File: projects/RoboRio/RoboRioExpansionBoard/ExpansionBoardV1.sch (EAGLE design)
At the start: 115 parts, among them IC1 MC1525TO, IC2 74HCT125N, Q1 5MHz

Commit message: Brokout 12 IO pins.
Was fun
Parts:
- removed IO0-SPI-CS, IO1-SPI-CLK, IO12, IO13, IO14, IO15, IO16, IO17, IO18, IO19, IO2-SPI-MOSI, IO20, IO21, IO22, IO23, IO24, IO25, IO26, IO27, IO3-SPI-MISO: (no value), con-lstb-modified:MA03-1
- added IO0, IO1, IO2, IO3: (no value), con-lstb-modified:MA03-1
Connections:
- new net IO28: IO5.3
- new net IO29: IO6.3
- new net IO30: IO7.3
- new net IO31: IO8.3
- new net IO32: IO9.3
- new net IO33: IO10.3
- new net IO34: IO11.3
- new net IO4: IO4.3
- net +3V3: now also IO0.2, IO1.2, IO2.2, IO3.2; no longer IO0-SPI-CS.2, IO1-SPI-CLK.2, IO12.2, IO13.2, IO14.2, IO15.2, IO16.2, IO17.2, IO18.2, IO19.2, IO2-SPI-MOSI.2, IO20.2, IO21.2, IO22.2, IO23.2, IO24.2, IO25.2, IO26.2, IO27.2, IO3-SPI-MISO.2
- net DGND: now also IO0.1, IO1.1, IO2.1, IO3.1; no longer IO0-SPI-CS.1, IO1-SPI-CLK.1, IO12.1, IO13.1, IO14.1, IO15.1, IO16.1, IO17.1, IO18.1, IO19.1, IO2-SPI-MOSI.1, IO20.1, IO21.1, IO22.1, IO23.1, IO24.1, IO25.1, IO26.1, IO27.1, IO3-SPI-MISO.1
- net IO0: now also IO0.3
- net IO1: now also IO1.3
- net IO10: no longer IO10.3
- net IO11: no longer IO11.3
- net IO12: no longer IO12.3
- net IO13: no longer IO13.3
- net IO14: no longer IO14.3
- net IO15: no longer IO15.3
- net IO16: no longer IO16.3
- net IO17: no longer IO17.3
- net IO18: no longer IO18.3
- net IO19: no longer IO19.3
- net IO2: now also IO2.3
- net IO20: no longer IO20.3
- net IO21: no longer IO21.3
- net IO22: no longer IO22.3
- net IO23: no longer IO23.3
- net IO24: no longer IO24.3
- net IO25: no longer IO25.3
- net IO26: no longer IO26.3
- net IO27: no longer IO27.3
- net IO3: now also IO3.3
- net IO4RRW: no longer IO4.3
- net IO5: no longer IO5.3
- net IO6: no longer IO6.3
- net IO7: no longer IO7.3
- net IO8: no longer IO8.3
- net IO9: no longer IO9.3
- net SPI_CLK: no longer IO1-SPI-CLK.3
- net SPI_CS: no longer IO0-SPI-CS.3
- net SPI_MISO: no longer IO3-SPI-MISO.3
- net SPI_MOSI: no longer IO2-SPI-MOSI.3
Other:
- moved on the sheet: IO10, IO11, IO4, IO5, IO6, IO7, IO8, IO9

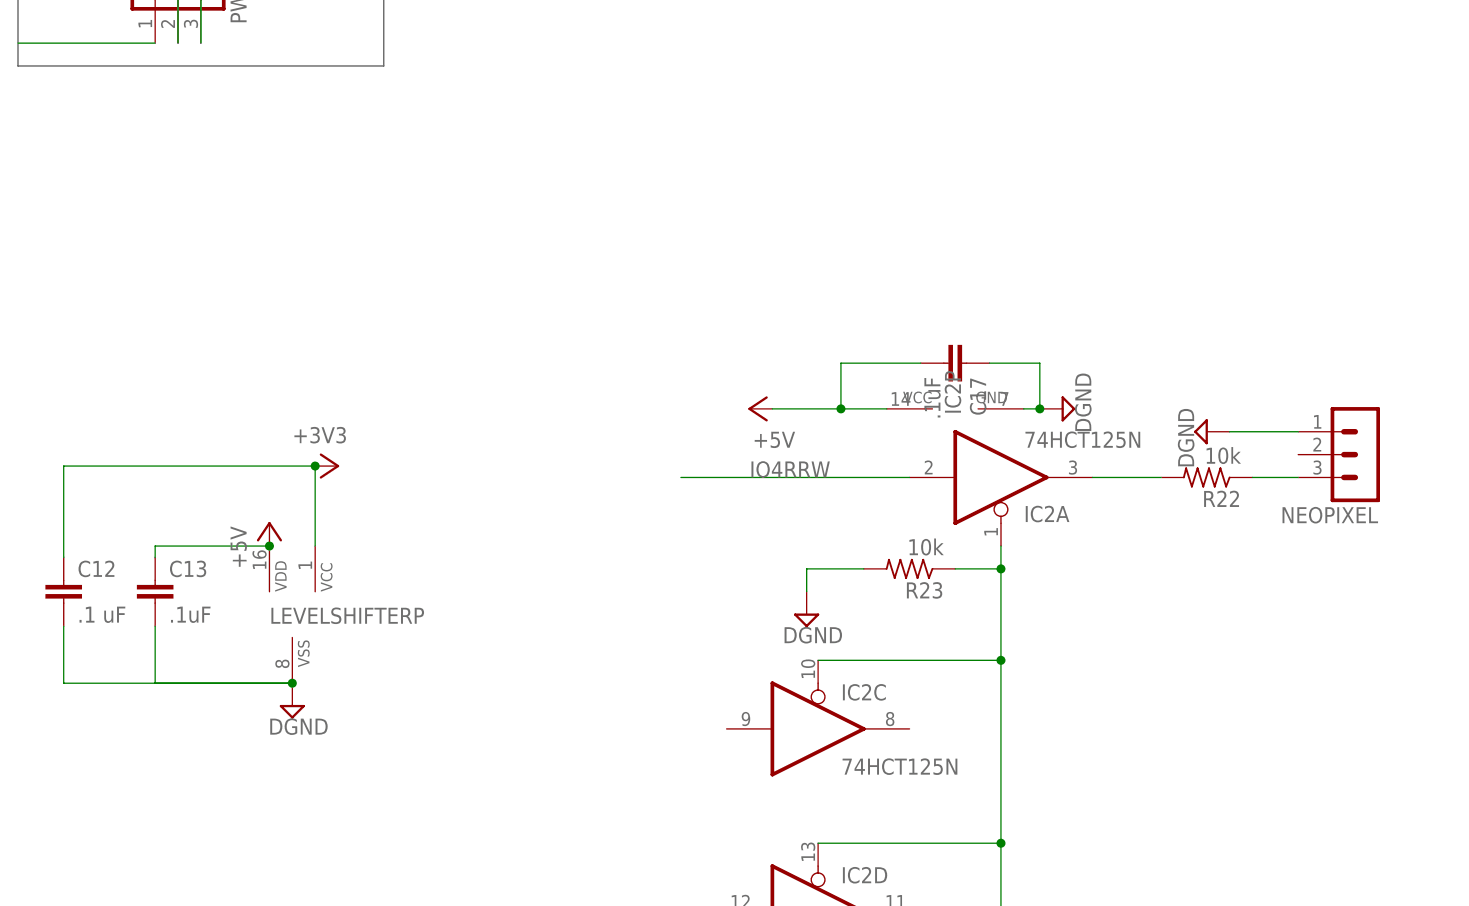
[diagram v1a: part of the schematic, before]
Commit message: Updated neopixel stuff
Not yet finished.
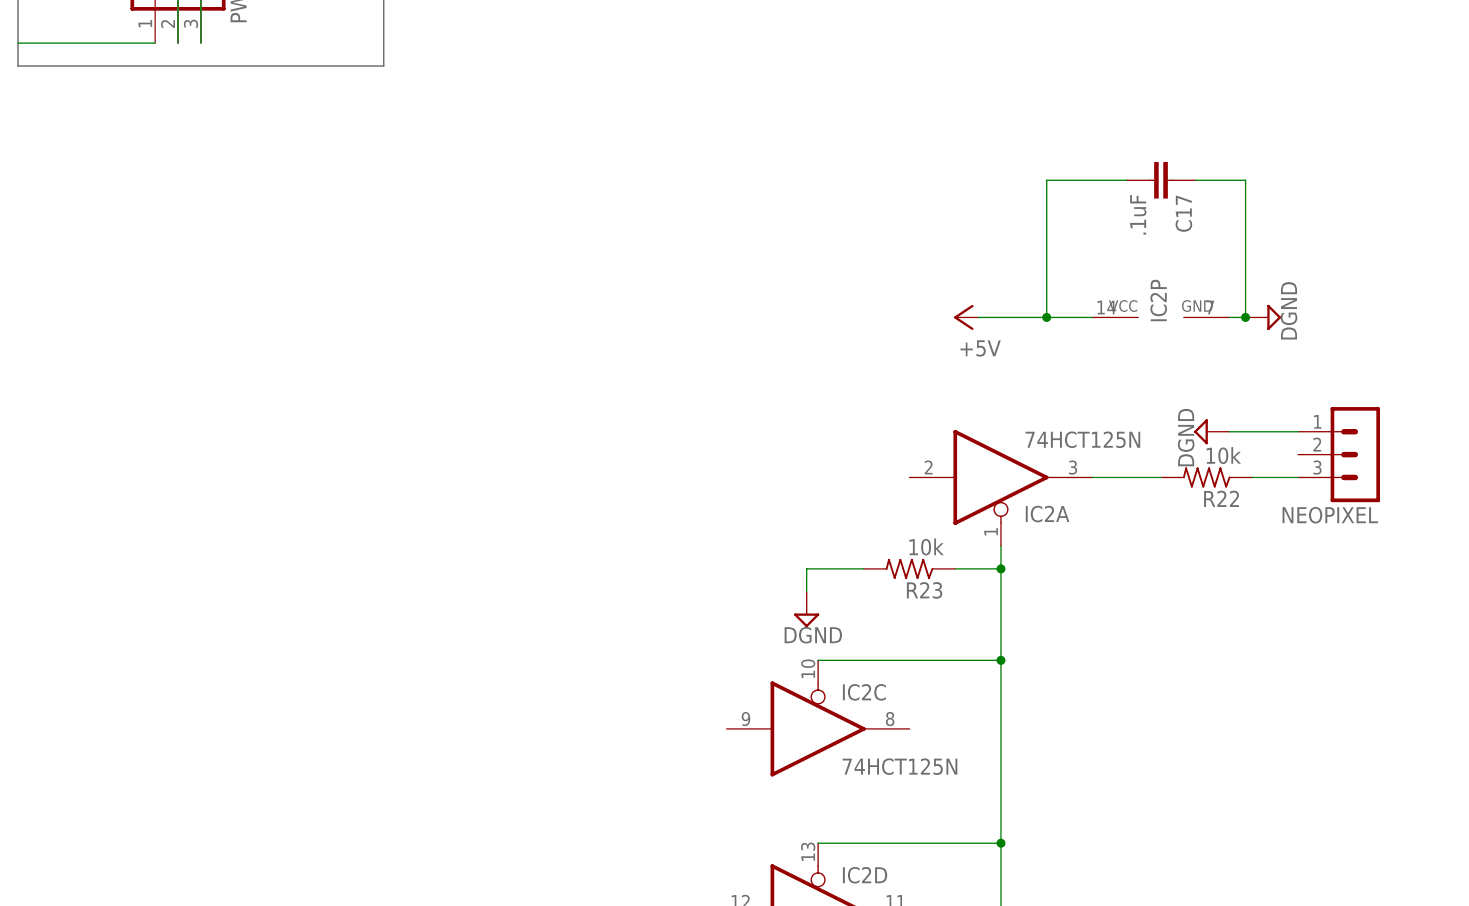
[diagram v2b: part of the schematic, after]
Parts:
- removed C12: .1 uF, capacitor-wima:C7.5/6
- removed C13: .1uF, capacitor-wima:C7.5/6
- removed LEVELSHIFTER: 40109, 40xx-2:40109
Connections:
- net +3V3: no longer C12.1, LEVELSHIFTERP.VCC
- net +5V: no longer C13.1, LEVELSHIFTERP.VDD
- net DGND: no longer C12.2, C13.2, LEVELSHIFTERP.VSS
- net IO4RRW: no longer IC2A.I
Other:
- moved on the sheet: C17, IC2P
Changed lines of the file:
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@@
 <part name="PWM9" library="con-lstb-modified" deviceset="MA03-1" device=""/>
 <part name="ADC" library="adafruit" deviceset="MCP3008" device=""/>
-<part name="LEVELSHIFTER" library="40xx-2" deviceset="40109" device=""/>
 <part name="NEOPIXEL" library="con-lstb-modified" deviceset="MA03-1" device=""/>
-<part name="P+12" library="supply1" deviceset="+5V" device=""/>
-<part name="+3V6" library="supply1" deviceset="+3V3" device=""/>
 <part name="R2" library="resistor" deviceset="R-US_" device="0309/V" value="150"/>
 <part name="R3" library="resistor" deviceset="R-US_" device="0309/V" value="150"/>
@@
 <part name="U$4" library="RESETBUTTON3000" deviceset="BUTTON" device=""/>
 <part name="C2" library="capacitor-wima" deviceset="C" device="7.5/6" value=".1uF"/>
-<part name="C12" library="capacitor-wima" deviceset="C" device="7.5/6" value=".1 uF"/>
-<part name="C13" library="capacitor-wima" deviceset="C" device="7.5/6" value=".1uF"/>
 <part name="AI2" library="con-lstb-modified" deviceset="MA03-1" device=""/>
 <part name="AI3" library="con-lstb-modified" deviceset="MA03-1" device=""/>
@@
 <part name="SUPPLY13" library="supply2" deviceset="DGND" device=""/>
 <part name="SUPPLY14" library="supply2" deviceset="DGND" device=""/>
-<part name="SUPPLY15" library="supply2" deviceset="DGND" device=""/>
 <part name="SUPPLY18" library="supply2" deviceset="DGND" device=""/>
 <part name="ADC0" library="con-lstb-modified" deviceset="MA03-1" device=""/>
@@
 <instance part="PWM9" gate="G$1" x="-355.6" y="0" rot="R270"/>
 <instance part="ADC" gate="G$1" x="-7.62" y="-83.82" rot="R180"/>
-<instance part="LEVELSHIFTER" gate="P" x="-342.9" y="-71.12"/>
 <instance part="NEOPIXEL" gate="G$1" x="-223.52" y="-53.34" rot="R180"/>
-<instance part="P+12" gate="1" x="-345.44" y="-60.96"/>
-<instance part="+3V6" gate="G$1" x="-337.82" y="-54.61" rot="R270"/>
 <instance part="R2" gate="G$1" x="-71.12" y="149.86" rot="R180"/>
 <instance part="R3" gate="G$1" x="-71.12" y="160.02" rot="R180"/>
@@
 <instance part="U$4" gate="G$1" x="27.94" y="101.6"/>
 <instance part="C2" gate="G$1" x="-55.88" y="68.58" rot="R90"/>
-<instance part="C12" gate="G$1" x="-368.3" y="-67.31"/>
-<instance part="C13" gate="G$1" x="-358.14" y="-67.31"/>
 <instance part="AI2" gate="G$1" x="-189.23" y="45.72" rot="R180"/>
 <instance part="AI3" gate="G$1" x="-189.23" y="31.75" rot="R180"/>
@@
 <instance part="SUPPLY13" gate="G$1" x="36.83" y="-27.94"/>
 <instance part="SUPPLY14" gate="G$1" x="-241.3" y="-50.8" rot="R270"/>
-<instance part="SUPPLY15" gate="G$1" x="-342.9" y="-81.28"/>
 <instance part="SUPPLY18" gate="G$1" x="-259.08" y="27.94"/>
 <instance part="ADC0" gate="G$1" x="71.12" y="-266.7" rot="R180"/>
@@
 <instance part="IC2" gate="C" x="-284.48" y="-83.82"/>
 <instance part="IC2" gate="D" x="-284.48" y="-104.14"/>
-<instance part="IC2" gate="P" x="-269.24" y="-48.26" rot="R90"/>
+<instance part="IC2" gate="P" x="-246.38" y="-38.1" rot="R90"/>
 <instance part="SUPPLY37" gate="G$1" x="-285.75" y="-71.12"/>
-<instance part="P+4" gate="1" x="-292.1" y="-48.26" rot="R90"/>
-<instance part="C17" gate="G$1" x="-267.97" y="-43.18" rot="R270"/>
-<instance part="SUPPLY38" gate="G$1" x="-257.302" y="-48.26" rot="R90"/>
+<instance part="P+4" gate="1" x="-269.24" y="-38.1" rot="R90"/>
+<instance part="C17" gate="G$1" x="-245.11" y="-22.86" rot="R270"/>
+<instance part="SUPPLY38" gate="G$1" x="-234.442" y="-38.1" rot="R90"/>
 <instance part="ADC1" gate="G$1" x="71.12" y="-236.22" rot="R180"/>
 <instance part="R6" gate="G$1" x="55.88" y="-238.76" rot="MR180"/>
@@
 </segment>
 <segment>
-<pinref part="LEVELSHIFTER" gate="P" pin="VCC"/>
-<pinref part="+3V6" gate="G$1" pin="+3V3"/>
-<pinref part="C12" gate="G$1" pin="1"/>
-<wire x1="-340.36" y1="-54.61" x2="-340.36" y2="-63.5" width="0.1524" layer="91"/>
-<junction x="-340.36" y="-54.61"/>
-<wire x1="-340.36" y1="-54.61" x2="-368.3" y2="-54.61" width="0.1524" layer="91"/>
-<wire x1="-368.3" y1="-54.61" x2="-368.3" y2="-64.77" width="0.1524" layer="91"/>
-</segment>
-<segment>
 <pinref part="U$6" gate="G$1" pin="VDD"/>
 <pinref part="+3V5" gate="G$1" pin="+3V3"/>
@@
 <wire x1="-83.82" y1="40.64" x2="-63.5" y2="40.64" width="0.1524" layer="91"/>
 <label x="-81.28" y="40.64" size="1.778" layer="95"/>
-</segment>
-<segment>
-<wire x1="-299.72" y1="-55.88" x2="-274.32" y2="-55.88" width="0.1524" layer="91"/>
-<label x="-292.1" y="-55.88" size="1.778" layer="95"/>
-<pinref part="IC2" gate="A" pin="I"/>
 </segment>
 </net>
@@
 </segment>
 <segment>
-<pinref part="LEVELSHIFTER" gate="P" pin="VDD"/>
-<pinref part="P+12" gate="1" pin="+5V"/>
-<wire x1="-345.44" y1="-63.5" x2="-358.14" y2="-63.5" width="0.1524" layer="91"/>
-<wire x1="-358.14" y1="-63.5" x2="-358.14" y2="-64.77" width="0.1524" layer="91"/>
-<pinref part="C13" gate="G$1" pin="1"/>
-<junction x="-345.44" y="-63.5"/>
-</segment>
-<segment>
 <pinref part="5V_LCD" gate="G$1" pin="2"/>
 <wire x1="33.02" y1="-34.29" x2="36.83" y2="-38.1" width="0.1524" layer="91"/>
@@
 <segment>
 <pinref part="P+4" gate="1" pin="+5V"/>
-<wire x1="-289.56" y1="-48.26" x2="-281.94" y2="-48.26" width="0.1524" layer="91"/>
-<wire x1="-281.94" y1="-48.26" x2="-281.94" y2="-43.18" width="0.1524" layer="91"/>
+<wire x1="-266.7" y1="-38.1" x2="-259.08" y2="-38.1" width="0.1524" layer="91"/>
+<wire x1="-259.08" y1="-38.1" x2="-259.08" y2="-22.86" width="0.1524" layer="91"/>
 <pinref part="C17" gate="G$1" pin="2"/>
-<wire x1="-273.05" y1="-43.18" x2="-281.94" y2="-43.18" width="0.1524" layer="91"/>
+<wire x1="-250.19" y1="-22.86" x2="-259.08" y2="-22.86" width="0.1524" layer="91"/>
 <pinref part="IC2" gate="P" pin="VCC"/>
-<wire x1="-281.94" y1="-48.26" x2="-276.86" y2="-48.26" width="0.1524" layer="91"/>
-<junction x="-281.94" y="-48.26"/>
+<wire x1="-259.08" y1="-38.1" x2="-254" y2="-38.1" width="0.1524" layer="91"/>
+<junction x="-259.08" y="-38.1"/>
 </segment>
 <segment>
@@
 </segment>
 <segment>
-<pinref part="LEVELSHIFTER" gate="P" pin="VSS"/>
-<pinref part="C12" gate="G$1" pin="2"/>
-<junction x="-342.9" y="-78.74"/>
-<wire x1="-342.9" y1="-78.74" x2="-368.3" y2="-78.74" width="0.1524" layer="91"/>
-<wire x1="-368.3" y1="-78.74" x2="-368.3" y2="-72.39" width="0.1524" layer="91"/>
-<pinref part="C13" gate="G$1" pin="2"/>
-<wire x1="-342.9" y1="-78.74" x2="-358.14" y2="-78.74" width="0.1524" layer="91"/>
-<wire x1="-358.14" y1="-78.74" x2="-358.14" y2="-72.39" width="0.1524" layer="91"/>
-<pinref part="SUPPLY15" gate="G$1" pin="DGND"/>
-</segment>
-<segment>
 <pinref part="U$1" gate="G$1" pin="8-DGND"/>
 <pinref part="U$1" gate="G$1" pin="16-DGND"/>
@@
 <segment>
 <pinref part="C17" gate="G$1" pin="1"/>
-<wire x1="-265.43" y1="-43.18" x2="-259.842" y2="-43.18" width="0.1524" layer="91"/>
+<wire x1="-242.57" y1="-22.86" x2="-236.982" y2="-22.86" width="0.1524" layer="91"/>
 <pinref part="IC2" gate="P" pin="GND"/>
-<wire x1="-259.842" y1="-43.18" x2="-259.842" y2="-48.26" width="0.1524" layer="91"/>
-<wire x1="-259.842" y1="-48.26" x2="-261.62" y2="-48.26" width="0.1524" layer="91"/>
+<wire x1="-236.982" y1="-22.86" x2="-236.982" y2="-38.1" width="0.1524" layer="91"/>
+<wire x1="-236.982" y1="-38.1" x2="-238.76" y2="-38.1" width="0.1524" layer="91"/>
 <pinref part="SUPPLY38" gate="G$1" pin="DGND"/>
-<junction x="-259.842" y="-48.26"/>
-</segment>
-<segment>
+<junction x="-236.982" y="-38.1"/>
+</segment>
+<segment>

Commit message: Were almost there......
"if your going through boring schematic checking, keep going"-Winston
Churchill
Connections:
- removed net IO28: IO5.3
- removed net IO29: IO6.3
- removed net IO30: IO7.3
- removed net IO31: IO8.3
- removed net IO32: IO9.3
- removed net IO33: IO10.3
- removed net IO34: IO11.3
- removed net IO4RRW: PROPELLERP8X32A-D40.P4
- removed net N$18: ADC.CH2
- removed net N$19: ADC.CH3
- removed net N$21: RN1.2, U$6.DAT2
- removed net N$23: C7.1, R11.1, R12.2
- removed net N$28: C8.1, R13.1, R14.2
- removed net N$32: C11.1, R20.1, R21.2
- removed net N$43: ADC.CH4
- removed net N$6: C4.1, R6.1, R8.2
- removed net SPI_CLK: U$1.21-IO5-SPI_CLK
- removed net SPI_CS: U$1.19-IO4-SPI_CS
- removed net SPI_MISO: U$1.23-IO4-SPI_MISO
- removed net SPI_MOSI: U$1.25-IO7-SPI_MOSI
- new net N$17: ADC.CH4, C8.1, R13.1, R14.2
- net IO0: now also U$1.19-IO4-SPI_CS
- net IO1: now also U$1.21-IO5-SPI_CLK
- net IO10: now also IO10.3
- net IO11: now also IO11.3
- net IO13: now also ADC.DIN
- net IO2: now also U$1.25-IO7-SPI_MOSI
- net IO3: now also U$1.23-IO4-SPI_MISO
- net IO4: now also PROPELLERP8X32A-D40.P4
- net IO5: now also IO5.3
- net IO6: now also IO6.3
- net IO7: now also IO7.3
- net IO8: now also IO8.3
- net IO9: now also IO9.3, U$6.DAT2
- net N$10: now also ADC.CH3, C7.1, R11.1, R12.2; no longer C5.1, R10.2, R9.1
- net N$16: now also ADC.CH2, C5.1, R10.2, R9.1; no longer ADC.DIN
- net N$8: now also C11.1, R20.1, R21.2
- net N$9: now also C4.1, R6.1, R8.2
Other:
- moved on the sheet: 5V_LCD, ADC, ADC0, ADC1, ADC2, ADC3, ADC4, ADC5, ADC6, ADC7, C10, C11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

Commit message: Updated Expansion board with various small issues
removed the neopixel circuit from the main board
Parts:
- removed C17: .1uF, capacitor-wima:C7.5/6
- removed GREEN2, GREEN3: (no value), led:LED5MM
- removed IC2: 74HCT125N, 74xx-eu:74HCT125N
- removed NEOPIXEL: (no value), con-lstb-modified:MA03-1
- removed R22, R23: 10k, resistor:R-US_0309/V
- added POWER3V3, POWER5V: (no value), led:LED5MM
- F1, F2: value (none) -> 1A
- RN1: value (none) -> 10k
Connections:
- removed net I2C_SCL: U$1.32-IO14-I2C_SCL
- removed net I2C_SDA: U$1.34-IO15-I2C_SDA
- removed net N$11: NEOPIXEL.3, R22.1
- removed net N$5: IC2A.O, R22.2
- removed net OE: IC2A.OE, IC2B.OE, IC2C.OE, IC2D.OE, R23.1
- removed net UART_RX: U$1.10-UART_RX
- removed net UART_TX: U$1.14-UART_TX
- net +5V: no longer C17.2, IC2P.VCC
- net DGND: now also POWER3V3.C, POWER5V.C; no longer C17.1, GREEN2.C, GREEN3.C, IC2P.GND, NEOPIXEL.1, R23.2
- net N$3: now also POWER3V3.A; no longer GREEN2.A
- net N$4: now also POWER5V.A; no longer GREEN3.A

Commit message: CHANGES COMING IS
CHANGE IS COMING
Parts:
- renumbered AI4 to AO0, AI5 to AO1
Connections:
- new net N$5: F2.2, U$1.P33-+3.3V
- net +3V3: no longer F2.2, U$1.P33-+3.3V
